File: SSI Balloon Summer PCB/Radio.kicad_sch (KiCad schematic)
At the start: 0 parts

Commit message: Worked on LoRa and APRS
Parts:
- added C13: 100nF, symbol Device:C
- added C14: 10uF, symbol Device:C
- added J3: Conn_Coaxial, symbol Connector:Conn_Coaxial
- added R6: 10k, symbol Device:R
- added U1: RFM95W-915S2, RFM95W-915S2:XCVR_RFM95W-915S2, symbol RFM95W-915S2:RFM95W-915S2
- added U5: DRA818V, DRA818V:DORJI_DRA818V, symbol DRA818V:DRA818V
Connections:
- new net: J3.1 (In), U1.9 (ANT)
- new net +3.3V: C13.2, C14.2, R6.2, U1.13 (3.3V)
- new net GND: C13.1, C14.1, J3.2 (Ext), U1.1 (GND), U1.10 (GND), U1.8 (GND), U5.10 (GND), U5.9 (GND)
- new net LoRa_CS: R6.1, U1.5 (NSS)
- new net LoRa_DIO0: U1.14 (DIO0)
- new net LoRa_RESET: U1.6 (RESET)
- new net MISO: U1.2 (MISO)
- new net MOSI: U1.3 (MOSI)
- new net SCK: U1.4 (SCK)
- no-connect marks 0 -> 5

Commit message: APRS work - MIC_IN pin left
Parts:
- added C23: 10uF, symbol Device:C
- added J4: Conn_Coaxial, symbol Connector:Conn_Coaxial
- added R11, R12: 10k, symbol Device:R
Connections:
- net GND: now also U5.7 (H/L), C23.1, J4.2 (Ext)
- net at U5.12 (ANT): now also J4.1 (In)
- net APRS_RXD: now reaches U5.16 (RXD)
- net APRS_TXD: now reaches U5.17 (TXD)
- net APRS_PTT: now reaches U5.5 (PTT)
- net APRS_PTT: now also R11.1
- net APRS_PD: now reaches U5.6 (PD)
- net APRS_PD: now also R12.1
- net +4V1: now reaches U5.8 (VBAT)
- net +4V1: now also C23.2
- new net +3V3: R11.2, R12.2
- no-connect marks 5 -> 7
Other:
- moved on the sheet: U5

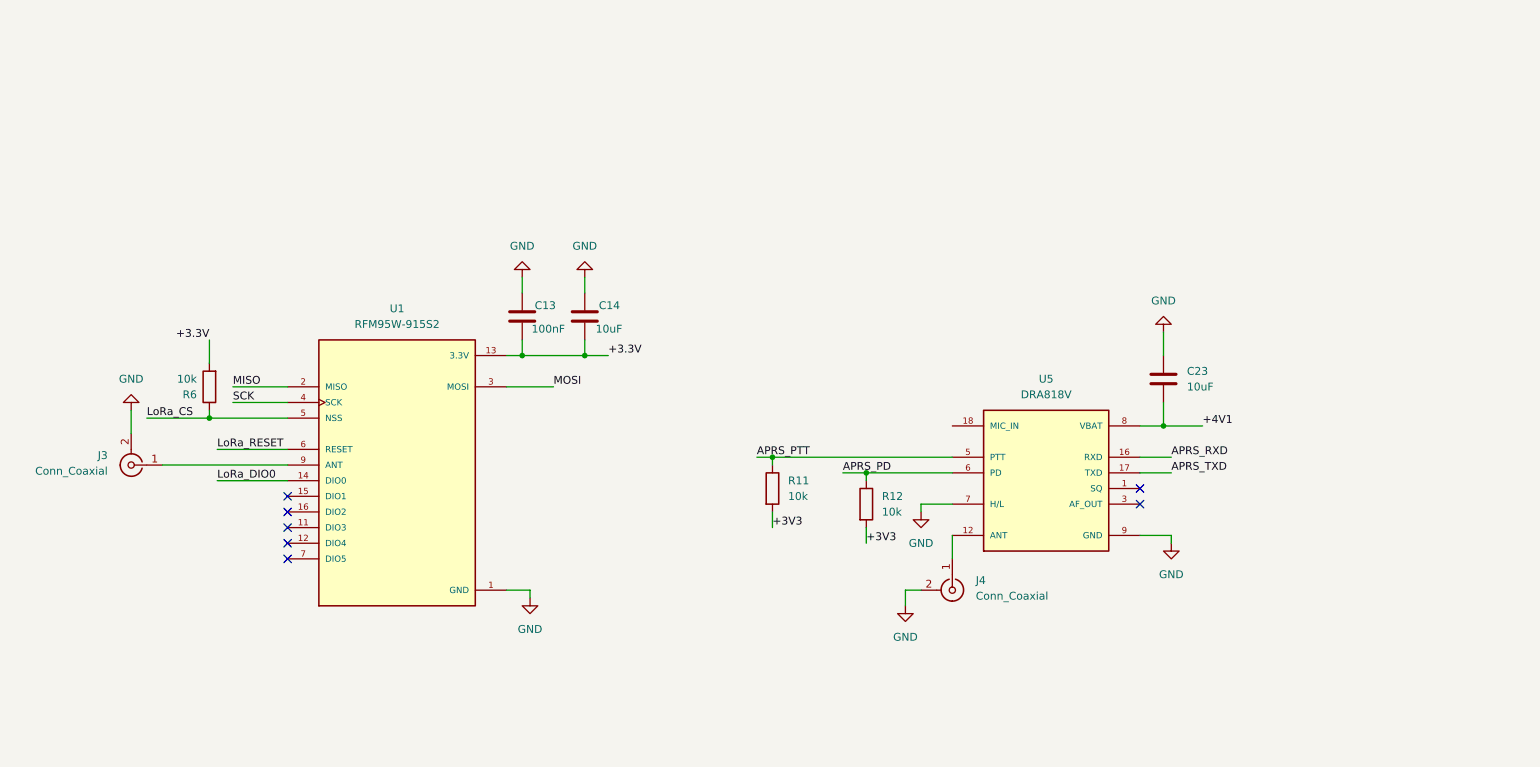
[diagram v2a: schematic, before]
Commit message: Standardized power symbols, added microSD sheet, and standardized hierarchical labels
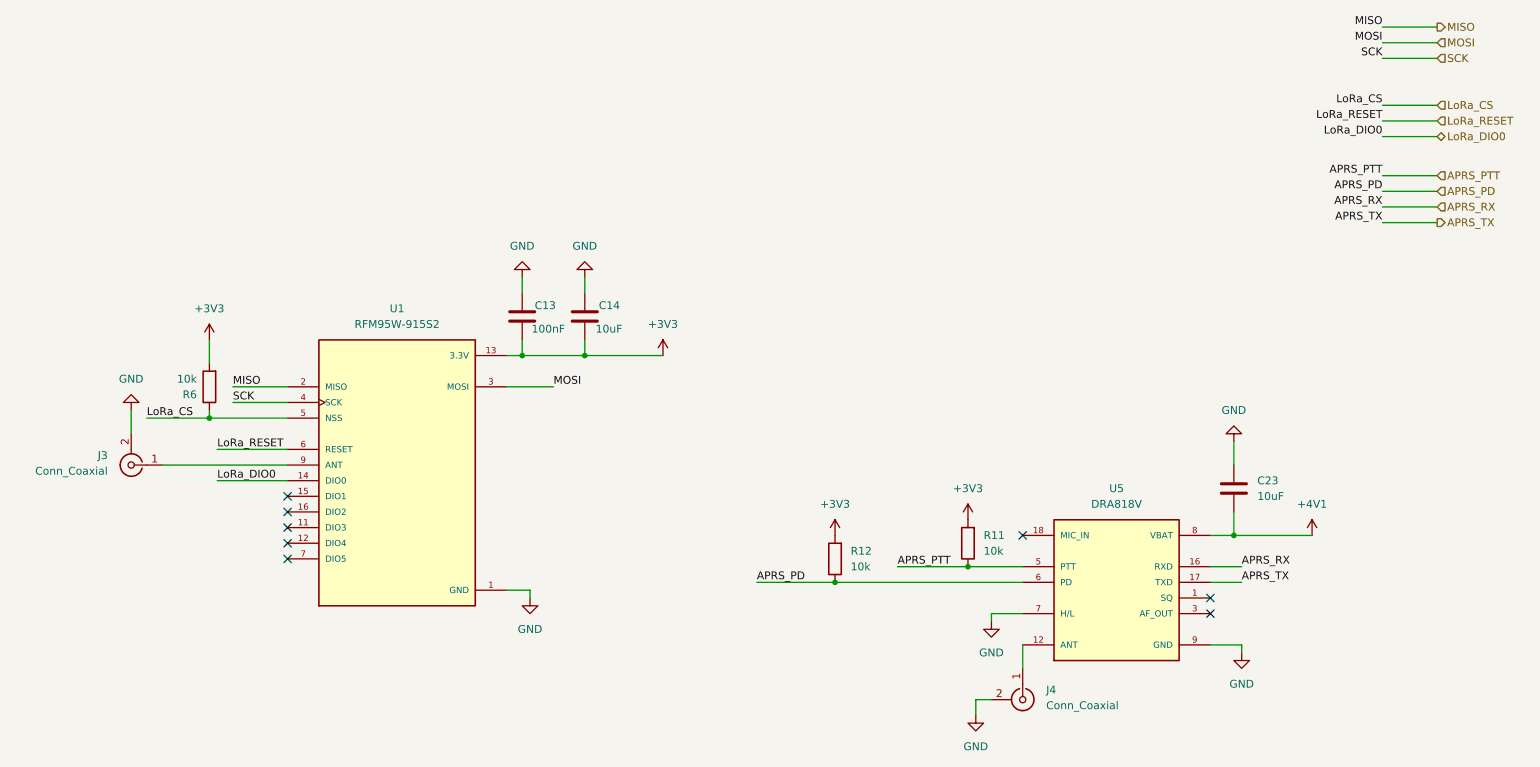
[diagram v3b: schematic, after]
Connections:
- net +3.3V is gone; now on net +3V3: C13.2, C14.2, R6.2, U1.13 (3.3V)
- net APRS_RXD renamed APRS_RX
- net APRS_TXD renamed APRS_TX
- no-connect marks 7 -> 8
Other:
- moved on the sheet: C23, J4, R11, R12, U5

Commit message: schematic
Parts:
- added C35: 10nF, symbol Device:C
- added C36, C37: 100nF, symbol Device:C
- added R18: 1k, symbol Device:R
- added R19: 10k, symbol Device:R
- added R20: 100, symbol Device:R
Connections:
- net +4V1: now also C37.2
- net GND: now also C35.2, C37.1, R20.2
- net at U5.18 (MIC_IN): now also R19.2, R20.1
- new net: C35.1, C36.1, R18.2
- new net: C36.2, R19.1
- new net APRS_AUDIO: R18.1
- no-connect marks 8 -> 7
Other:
- moved on the sheet: C23, R12

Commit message: Finished GPS
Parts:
- J3: value Conn_Coaxial -> LoRa antenna
- J4: value Conn_Coaxial -> APRS antenna
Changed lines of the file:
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@@
 			)
 		)
-		(property "Value" "Conn_Coaxial"
+		(property "Value" "LoRa antenna"
 			(at 48.26 92.4167 0)
 			(show_name no)
@@
 			)
 		)
-		(property "Value" "Conn_Coaxial"
+		(property "Value" "APRS antenna"
 			(at 200.66 130.4924 90)
 			(show_name no)

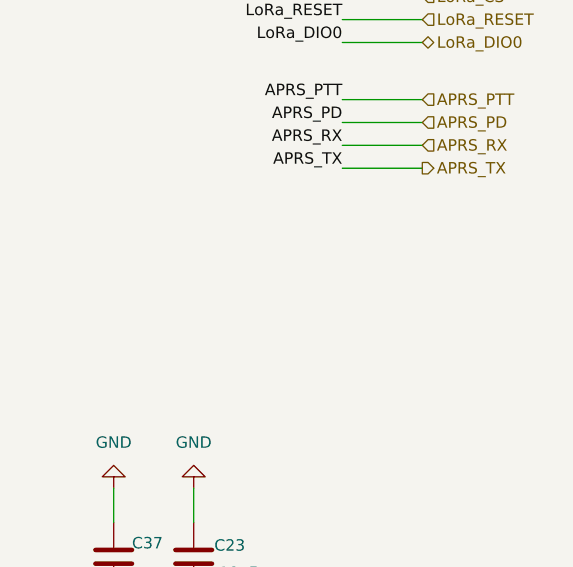
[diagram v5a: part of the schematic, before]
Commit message: Tidied some labels up
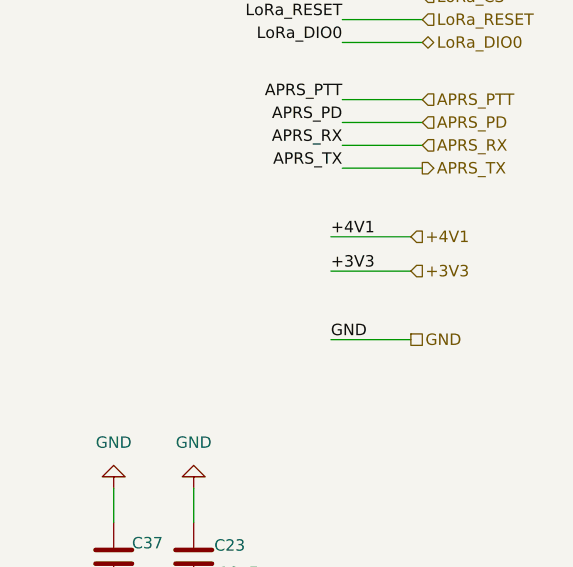
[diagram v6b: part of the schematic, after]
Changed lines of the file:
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@@
+	(wire
+		(pts
+			(xy 254 63.5) (xy 262.89 63.5)
+		)
+		(stroke
+			(width 0)
+			(type default)
+		)
+	)
 	(wire
 		(pts
@@
 	(wire
 		(pts
+			(xy 254 71.12) (xy 262.89 71.12)
+		)
+		(stroke
+			(width 0)
+			(type default)
+		)
+	)
+	(wire
+		(pts
 			(xy 255.27 33.02) (xy 264.16 33.02)
 		)
@@
 		(pts
 			(xy 187.96 107.95) (xy 196.85 107.95)
+		)
+		(stroke
+			(width 0)
+			(type default)
+		)
+	)
+	(wire
+		(pts
+			(xy 254 59.69) (xy 262.89 59.69)
 		)
 		(stroke
@@
 		)
 	)
+	(label "+4V1"
+		(at 254 59.69 0)
+		(effects
+			(font
+				(size 1.27 1.27)
+			)
+			(justify left bottom)
+		)
+	)
 	(label "MOSI"
 		(at 120.65 78.74 0)
@@
 		)
 	)
+	(label "GND"
+		(at 254 71.12 0)
+		(effects
+			(font
+				(size 1.27 1.27)
+			)
+			(justify left bottom)
+		)
+	)
 	(label "LoRa_CS"
 		(at 255.27 33.02 180)
@@
 	(label "APRS_AUDIO"
 		(at 147.32 80.01 0)
+		(effects
+			(font
+				(size 1.27 1.27)
+			)
+			(justify left bottom)
+		)
+	)
+	(label "+3V3"
+		(at 254 63.5 0)
 		(effects
 			(font
@@
 		)
 	)
+	(hierarchical_label "+3V3"
+		(shape input)
+		(at 262.89 63.5 0)
+		(effects
+			(font
+				(size 1.27 1.27)
+			)
+			(justify left)
+		)
+	)
 	(hierarchical_label "LoRa_CS"
 		(shape input)
@@
 		(effects
 			(font
+				(size 1.27 1.27)
+			)
+			(justify left)
+		)
+	)
+	(hierarchical_label "GND"
+		(shape passive)
+		(at 262.89 71.12 0)
+		(effects
+			(font
+				(size 1.27 1.27)
+			)
+			(justify left)
+		)
+	)
+	(hierarchical_label "+4V1"
+		(shape input)
+		(at 262.89 59.69 0)
+		(effects
+			(font
